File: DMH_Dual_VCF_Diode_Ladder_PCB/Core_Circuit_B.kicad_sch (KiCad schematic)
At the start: 43 parts, among them SW4 SW_SPDT, SW5 SW_SPDT, SW6 SW_SPDT, U3 TL074, U4 TL074, U5 TL074, U6 TL074

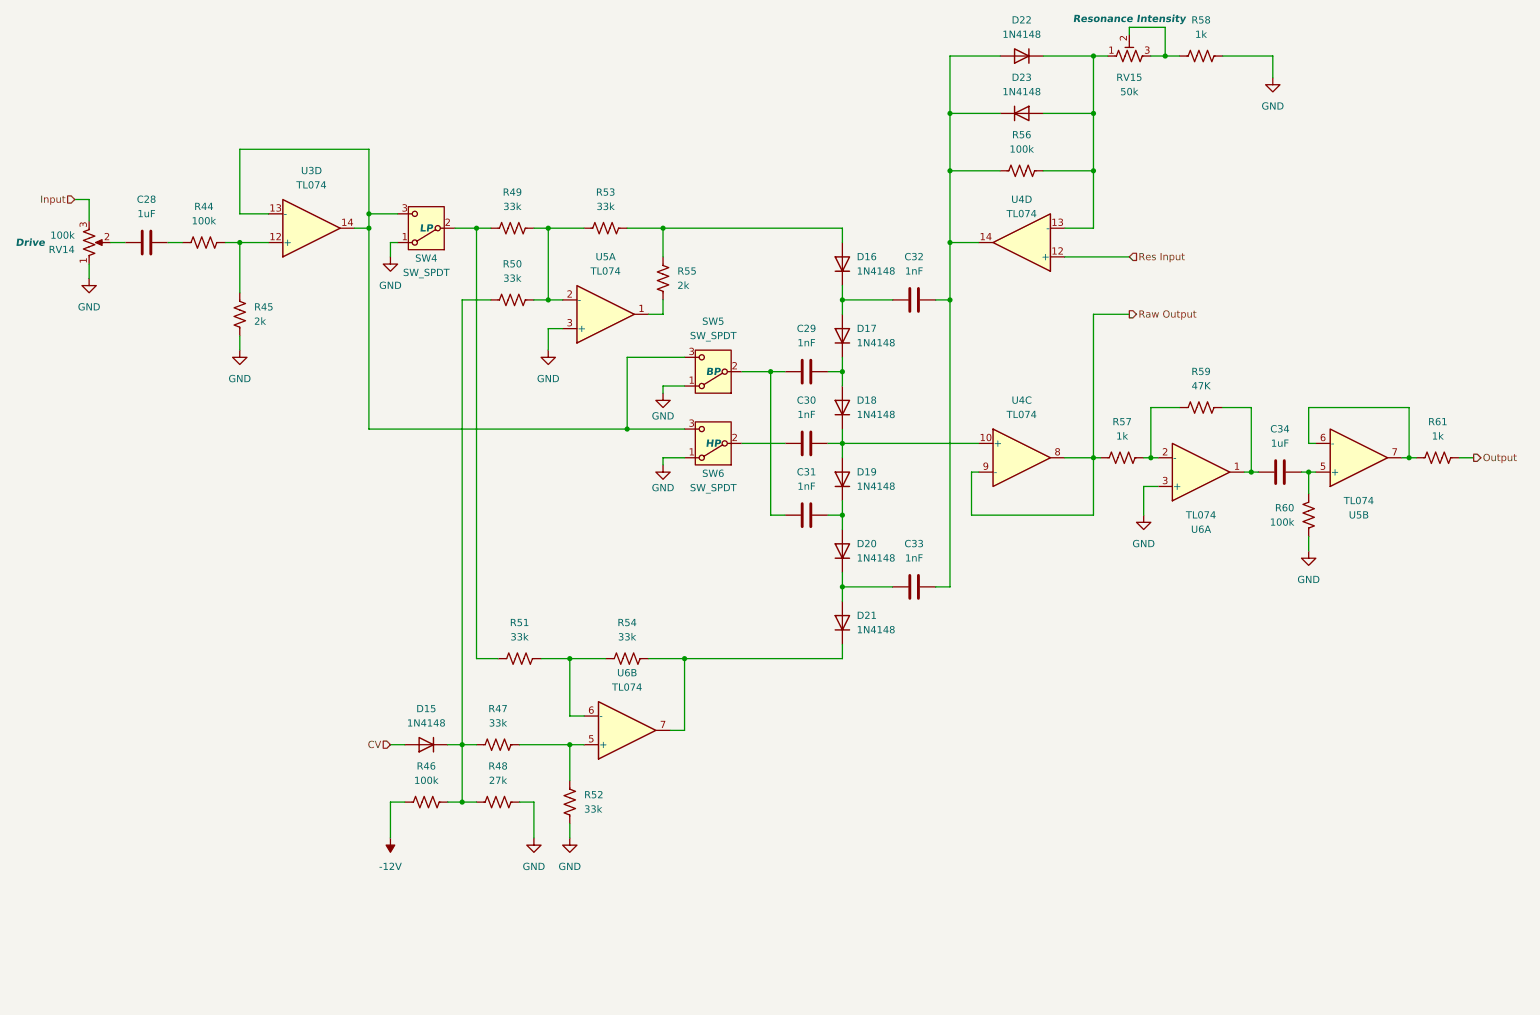
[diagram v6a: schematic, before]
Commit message: Re-annotated OpAmps as per PCB layout
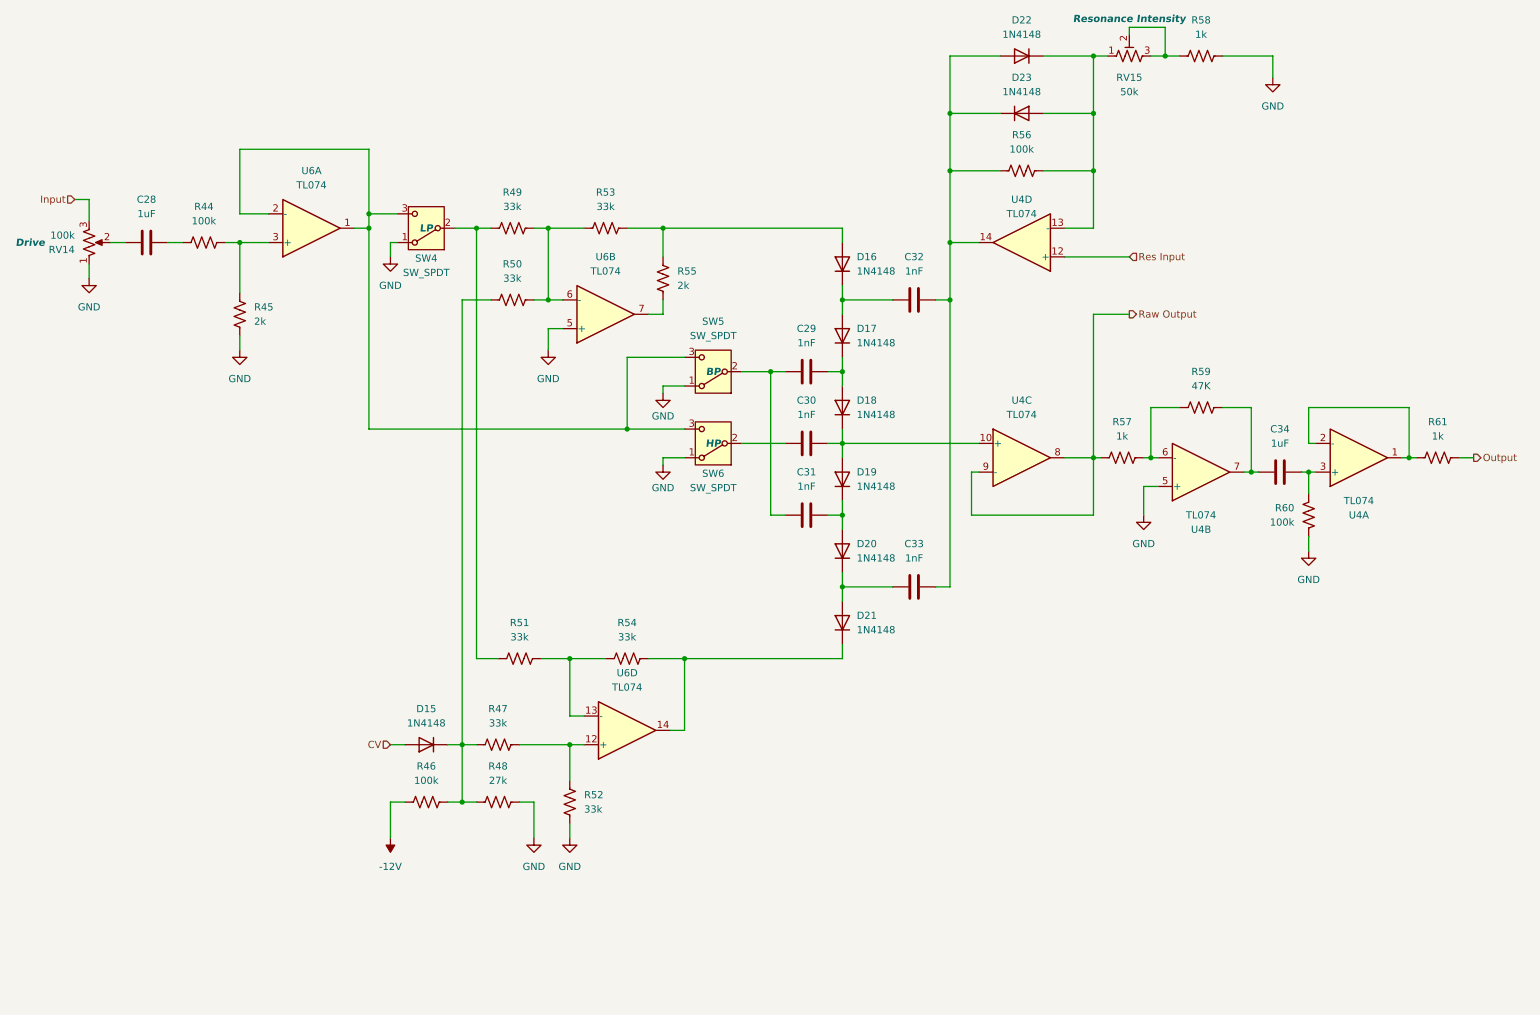
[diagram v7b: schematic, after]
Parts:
- renumbered U5 to U4, U6 to U4, U5 to U6, U3 to U6
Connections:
- net GND: now also U4.5 (+), U6.5 (+); no longer U4.3 (+), U6.3 (+)
- net at R44.2, R45.2: now also U6.3 (+); no longer U6.12 (+)
- net at R55.1: now also U6.7; no longer U6.1
- net at R49.2, R50.2, R53.1: now also U6.6 (-); no longer U6.2 (-)
- net at SW4.3 (C), SW5.3 (C), SW6.3 (C): now also U6.1, U6.2 (-); no longer U6.13 (-), U6.14
- net at R51.2, R54.1: now also U6.13 (-); no longer U6.6 (-)
- net at R47.2, R52.2: now also U6.12 (+); no longer U6.5 (+)
- net at C34.2, R60.2: now also U4.3 (+); no longer U4.5 (+)
- net at C34.1, R59.2: now also U4.7; no longer U4.1
- net at R57.2, R59.1: now also U4.6 (-); no longer U4.2 (-)
- net at D21.1 (K), R54.2: now also U6.14; no longer U6.7
- new net: R61.1, U4.1, U4.2 (-)
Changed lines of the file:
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@@
 		(at 250.19 101.6 0)
 		(mirror x)
-		(unit 2)
-		(exclude_from_sim no)
-		(in_bom yes)
-		(on_board yes)
-		(dnp no)
-		(property "Reference" "U5"
+		(unit 1)
+		(exclude_from_sim no)
+		(in_bom yes)
+		(on_board yes)
+		(dnp no)
+		(property "Reference" "U4"
 			(at 250.19 111.76 0)
 			(effects
@@
 			(project "DMH_Dual_VCF_Diode_Ladder_PCB"
 				(path "/58f4306d-5387-4983-bb08-41a2313fd315/5770dcd3-eb9e-472f-b743-1e3eb22ed082"
-					(reference "U5")
-					(unit 2)
+					(reference "U4")
+					(unit 1)
 				)
 			)
@@
 		(at 222.25 104.14 0)
 		(mirror x)
-		(unit 1)
-		(exclude_from_sim no)
-		(in_bom yes)
-		(on_board yes)
-		(dnp no)
-		(property "Reference" "U6"
+		(unit 2)
+		(exclude_from_sim no)
+		(in_bom yes)
+		(on_board yes)
+		(dnp no)
+		(property "Reference" "U4"
 			(at 222.25 114.3 0)
 			(effects
@@
 			(project "DMH_Dual_VCF_Diode_Ladder_PCB"
 				(path "/58f4306d-5387-4983-bb08-41a2313fd315/5770dcd3-eb9e-472f-b743-1e3eb22ed082"
-					(reference "U6")
-					(unit 1)
+					(reference "U4")
+					(unit 2)
 				)
 			)
@@
 		(at 116.84 76.2 0)
 		(mirror x)
-		(unit 1)
-		(exclude_from_sim no)
-		(in_bom yes)
-		(on_board yes)
-		(dnp no)
-		(fields_autoplaced yes)
-		(property "Reference" "U5"
+		(unit 2)
+		(exclude_from_sim no)
+		(in_bom yes)
+		(on_board yes)
+		(dnp no)
+		(fields_autoplaced yes)
+		(property "Reference" "U6"
 			(at 116.84 66.04 0)
 			(effects
@@
 			(project "DMH_Dual_VCF_Diode_Ladder_PCB"
 				(path "/58f4306d-5387-4983-bb08-41a2313fd315/5770dcd3-eb9e-472f-b743-1e3eb22ed082"
-					(reference "U5")
-					(unit 1)
+					(reference "U6")
+					(unit 2)
 				)
 			)
@@
 		(at 120.65 149.86 0)
 		(mirror x)
-		(unit 2)
+		(unit 4)
 		(exclude_from_sim no)
 		(in_bom yes)
@@
 				(path "/58f4306d-5387-4983-bb08-41a2313fd315/5770dcd3-eb9e-472f-b743-1e3eb22ed082"
 					(reference "U6")
-					(unit 2)
+					(unit 4)
 				)
 			)
@@
 		(at 64.77 60.96 0)
 		(mirror x)
-		(unit 4)
-		(exclude_from_sim no)
-		(in_bom yes)
-		(on_board yes)
-		(dnp no)
-		(fields_autoplaced yes)
-		(property "Reference" "U3"
+		(unit 1)
+		(exclude_from_sim no)
+		(in_bom yes)
+		(on_board yes)
+		(dnp no)
+		(fields_autoplaced yes)
+		(property "Reference" "U6"
 			(at 64.77 50.8 0)
 			(effects
@@
 			(project "DMH_Dual_VCF_Diode_Ladder_PCB"
 				(path "/58f4306d-5387-4983-bb08-41a2313fd315/5770dcd3-eb9e-472f-b743-1e3eb22ed082"
-					(reference "U3")
-					(unit 4)
-				)
-			)
+					(reference "U6")
+					(unit 1)
+				)
+			)

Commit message: Finished routing
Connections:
- net GND: now also SW4.3 (C), SW5.3 (C), SW6.3 (C); no longer SW4.1 (A), SW5.1 (A), SW6.1 (A)
- new net: SW4.1 (A), SW5.1 (A), SW6.1 (A), U6.1, U6.2 (-)
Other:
- moved on the sheet: SW4, SW5, SW6
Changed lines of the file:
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@@
 	(symbol
 		(lib_id "Switch:SW_SPDT")
-		(at 135.89 86.36 180)
-		(unit 1)
-		(exclude_from_sim no)
-		(in_bom yes)
-		(on_board yes)
-		(dnp no)
-		(fields_autoplaced yes)
+		(at 135.89 86.36 0)
+		(mirror y)
+		(unit 1)
+		(exclude_from_sim no)
+		(in_bom yes)
+		(on_board yes)
+		(dnp no)
 		(property "Reference" "SW5"
-			(at 135.89 77.47 0)
+			(at 135.89 81.28 0)
 			(effects
 				(font
@@
 		)
 		(property "Value" "SW_SPDT"
-			(at 135.89 80.01 0)
+			(at 135.89 91.694 0)
 			(effects
 				(font
@@
 		)
 		(property "Datasheet" "~"
-			(at 135.89 78.74 0)
+			(at 135.89 93.98 0)
 			(effects
 				(font
@@
 	(symbol
 		(lib_id "Switch:SW_SPDT")
-		(at 135.89 99.06 180)
+		(at 135.89 99.06 0)
+		(mirror y)
 		(unit 1)
 		(exclude_from_sim no)
@@
 		(dnp no)
 		(property "Reference" "SW6"
+			(at 135.89 93.726 0)
+			(effects
+				(font
+					(size 1.27 1.27)
+				)
+			)
+		)
+		(property "Value" "SW_SPDT"
 			(at 135.89 104.394 0)
-			(effects
-				(font
-					(size 1.27 1.27)
-				)
-			)
-		)
-		(property "Value" "SW_SPDT"
-			(at 135.89 106.934 0)
 			(effects
 				(font
@@
 		)
 		(property "Datasheet" "~"
-			(at 135.89 91.44 0)
+			(at 135.89 106.68 0)
 			(effects
 				(font
@@
 	(symbol
 		(lib_id "Switch:SW_SPDT")
-		(at 85.09 60.96 180)
+		(at 85.09 60.96 0)
+		(mirror y)
 		(unit 1)
 		(exclude_from_sim no)
@@
 		(dnp no)
 		(property "Reference" "SW4"
-			(at 85.09 66.294 0)
+			(at 85.09 55.626 0)
 			(effects
 				(font
@@
 		)
 		(property "Value" "SW_SPDT"
-			(at 85.09 68.834 0)
+			(at 85.09 53.086 0)
 			(effects
 				(font
@@
 		)
 		(property "Datasheet" "~"
-			(at 85.09 53.34 0)
-			(effects
-				(font
+			(at 85.09 68.58 0)
+			(effects
+				(font
